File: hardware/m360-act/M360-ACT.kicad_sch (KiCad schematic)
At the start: 26 parts, among them J1 5V do quadro, J2 M360-RF, J3 RJ45 RELES-A, J4 RJ45 RELES-B, J5 RJ45 SENSORES, SW1 Reed, U1 AMS1117-3.3, U2 74HCT244, U3 CD74HC4067, U4 SRV05-4, U5 SRV05-4, U6 SRV05-4, U7 SRV05-4, U8 SRV05-4

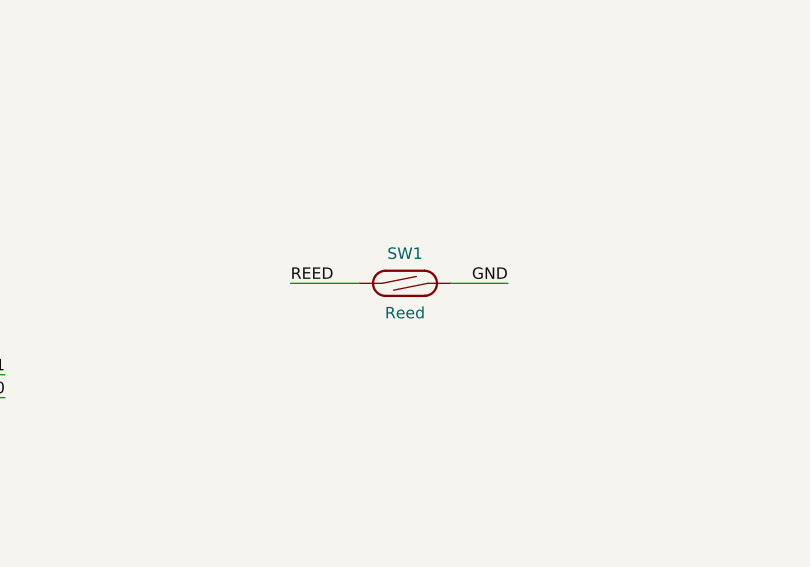
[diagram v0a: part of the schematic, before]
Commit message: feat(hardware): reed vira botão na LP e na ACT — esquemático apenas
⚠️ **ENTREGA PARCIAL: as placas NÃO acompanham.** Os dois `.kicad_pcb` continuam com o reed
`M360:Reed_Littelfuse_59170`. Sincronizar esquemático → placa vai trocar o footprint e
**invalidar o roteamento das duas** (§11.5). Não faça isso sem estar pronto para rerrotear.

O que entra aqui:

- SW1 passa de `Switch:SW_Reed` para `Switch:SW_Push`, footprint
  `Button_Switch_THT:SW_PUSH_6mm`, valor "Repareamento". Os dois símbolos têm pinagem e
  geometria idênticas (pinos 1 e 2 em ±5,08), então a troca não pode alterar a fiação — e o
  `netdiff.py` confirmou: LP 47 redes/182 nós e ACT 63/166, idênticas à base nas duas;
- `place_lp.py`: SW1 de (160, 158) para (160, 153) — o botão ocupa 9,6 × 7,6 mm contra
  11,5 × 2,4 do reed e, em 158, avançaria até y ≈ 164, além da borda em 162;
- `place_act.py`: SW1 sem rotação, e **J1 de rot 90 para rot 0**. O borne abre para −x (as guias
  de fio estão em x ≈ −5,68 no footprint), então em rot 90 a abertura apontava para dentro da
  placa;
- `.kicad_pro` das duas: `track_width` de 0,2 para 0,25 mm, o padrão da família (§11.2). O
  `set_design_rules` do MCP nunca persistiu esse valor — gravava o mínimo.

**Por que parou aqui.** A troca do footprint exige rerroteamento completo, que depende de
`export_dsn`/`import_ses` — e o servidor MCP travou no meio do trabalho: até `get_board_info`
passou a estourar 30 s, dez sondagens seguidas. O `kicad-cli` não exporta nem importa Specctra,
então não há contorno. As placas foram revertidas ao estado commitado e íntegro (LP 552
segmentos/48 vias, ACT 463/23, conferidos contra `bf701dc` e `e94779f`).

Ferramentas novas, todas nascidas deste trabalho:

- `clear_tracks.py` — apaga trilhas e vias para rerrotear do zero;
- `zone_thermals.py` — afina o alívio térmico das zonas;
- `gnd_stitch.py` — via de costura em ilha de plano solta, **com defeito conhecido e
  documentado**: o critério interno de "ilha já ligada" não prova ligação ao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
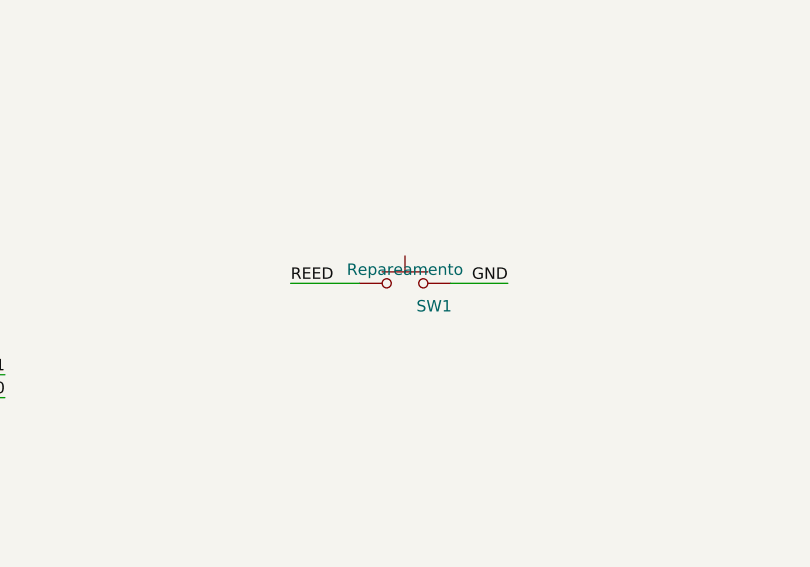
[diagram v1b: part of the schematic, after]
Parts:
- removed SW1: Reed, M360:Reed_Littelfuse_59170, symbol Switch:SW_Reed
- added SW1: Repareamento, Button_Switch_THT:SW_PUSH_6mm, symbol Switch:SW_Push
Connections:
- net GND: now also SW1.2
- net REED: now also SW1.1
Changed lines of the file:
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@@
 	)
 	(symbol
-		(lib_id "Switch:SW_Reed")
-		(at 124.46 209.55 0)
-		(unit 1)
-		(body_style 1)
-		(exclude_from_sim no)
-		(in_bom yes)
-		(on_board yes)
-		(in_pos_files yes)
-		(dnp no)
-		(property "Reference" "SW1"
-			(at 124.46 206.248 0)
-			(show_name no)
-			(do_not_autoplace no)
-			(effects
-				(font
-					(size 1.27 1.27)
-				)
-			)
-		)
-		(property "Value" "Reed"
-			(at 124.46 212.852 0)
-			(show_name no)
-			(do_not_autoplace no)
-			(effects
-				(font
-					(size 1.27 1.27)
-				)
-			)
-		)
-		(property "Footprint" "M360:Reed_Littelfuse_59170"
-			(at 124.46 209.55 0)
-			(hide yes)
-			(show_name no)
-			(do_not_autoplace no)
-			(effects
-				(font
-					(size 1.27 1.27)
-				)
-			)
-		)
-		(property "Datasheet" ""
-			(at 124.46 209.55 0)
-			(hide yes)
-			(show_name no)
-			(do_not_autoplace no)
-			(effects
-				(font
-					(size 1.27 1.27)
-				)
-			)
-		)
-		(property "Description" "reed switch"
-			(at 124.46 209.55 0)
-			(hide yes)
-			(show_name no)
-			(do_not_autoplace no)
-			(effects
-				(font
-					(size 1.27 1.27)
-				)
-			)
-		)
-		(pin "1"
-		)
-		(pin "2"
-		)
-		(instances
-			(project "M360-ACT"
-				(path "/c5ce62f1-25ea-4dcc-94a9-6f847c324d30"
-					(reference "SW1")
-					(unit 1)
-				)
-			)
-		)
-	)
-	(symbol
 		(lib_id "74xx:74HCT244")
 		(at 165.1 124.46 0)
@@
 		)
 	)
+	(symbol
+		(lib_id "Switch:SW_Push")
+		(at 124.46 209.55 0)
+		(unit 1)
+		(body_style 1)
+		(exclude_from_sim no)
+		(in_bom yes)
+		(on_board yes)
+		(in_pos_files yes)
+		(dnp no)
+		(property "Reference" "SW1"
+			(at 125.73 212.09 0)
+			(show_name no)
+			(do_not_autoplace no)
+			(effects
+				(font
+					(size 1.27 1.27)
+				)
+				(justify left)
+			)
+		)
+		(property "Value" "Repareamento"
+			(at 124.46 208.026 0)
+			(show_name no)
+			(do_not_autoplace no)
+			(effects
+				(font
+					(size 1.27 1.27)
+				)
+			)
+		)
+		(property "Footprint" "Button_Switch_THT:SW_PUSH_6mm"
+			(at 124.46 214.63 0)
+			(hide yes)
+			(show_name no)
+			(do_not_autoplace no)
+			(effects
+				(font
+					(size 1.27 1.27)
+				)
+			)
+		)
+		(property "Datasheet" ""
+			(at 124.46 214.63 0)
+			(hide yes)
+			(show_name no)
+			(do_not_autoplace no)
+			(effects
+				(font
+					(size 1.27 1.27)
+				)
+			)
+		)
+		(property "Description" "Push button switch, generic, two pins"
+			(at 124.46 209.55 0)
+			(hide yes)
+			(show_name no)
+			(do_not_autoplace no)
+			(effects
+				(font
+					(size 1.27 1.27)
+				)
+			)
+		)
+		(pin "1"
+		)
+		(pin "2"
+		)
+		(instances
+			(project "M360-ACT"
+				(path "/c5ce62f1-25ea-4dcc-94a9-6f847c324d30"
+					(reference "SW1")
+					(unit 1)
+				)
+			)
+		)
+	)

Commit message: feat(hardware): LP e ACT rerroteadas com o botão; GND volta a ser roteado
Conclui a troca do reed pelo botão iniciada em 0948368, que parou no esquemático.

Placas, para cada uma: del_fp.py SW1 → sincronização com o esquemático → place_*.py →
clear_tracks.py → export_dsn → dsn_sem_plano.py → Freerouting → import_ses →
zone_thermals.py → DRC com refill.

- M360-LP: 572 trilhas, 44 vias. DRC com 0 erros e 0 desconectados; restam os 8
  silk_edge_clearance dos RJ45, que já existiam.
- M360-ACT: 489 trilhas, 24 vias. DRC com 0 erros e 0 desconectados; restam os 13
  silk_edge_clearance, que já existiam. J1 em rot 0, como o place_act.py já pedia.
- Redes de todos os pads conferidas contra o HEAD: só o SW1 mudou. Trilhas todas de 0,25 mm.
- Paridade esquemático × placa com as mesmas contagens da base (237 e 195); some o
  footprint_symbol_mismatch do SW1.

**O GND não era roteado — e era isso que partia o plano.** Com zona de GND na placa, o DSN
declara `plane GND` e o Freerouting não desenha um fio de terra sequer. O primeiro roteamento
(bf701dc, 88 segmentos de GND) foi feito antes de as zonas existirem; todo rerroteamento
posterior perdia esse terra. Rerroteada com o DSN como sai do KiCad, a LP deu 16
unconnected_items, todos "Zona [GND]"; tirando as declarações plane, 0 — 100 segmentos de GND
na LP e 95 na ACT. Explica também os 15 desconectados imóveis da sessão anterior (§11.6).
Novo `tools/dsn_sem_plano.py`, e a §11 corrigida: 11.2, 11.4, 11.5 e 11.6.

Ajustes que o DRC pediu depois do rerroteamento:
- J4 da ACT, pino 8: starved_thermal → ligação sólida (pad_zone_connect.py), como o J3;
- silk_lp.py: referência do SW1 saía sobre "M360-LP"; vai para (172, 155);
- silk_act.py: referência do U1 encostava no J1, agora em rot 0; sobe para y = 143.

Botão: SHOU HAN TS665CJ, C393938, tátil 6 × 6 mm THT, SW1 nas três placas (LP, ACT e GW),
**solda manual e fora do PCBA**. Propriedade LCSC gravada nos três esquemáticos, com netlists
idênticas antes e depois. `add_lcsc.py` g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
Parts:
- SW1: LCSC (none) -> C393938
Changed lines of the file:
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@@
+			)
+		)
+		(property "LCSC" "C393938"
+			(at 124.46 209.55 0)
+			(hide yes)
+			(effects
+				(font
+					(size 1.27 1.27)
+				)
 			)
 		)

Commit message: feat(hardware): peças de solda manual fora do BOM e da posição; C13 da LP corrigido
Novo `tools/solda_manual.py`: marca as duas pontas pela referência — `in_bom no` e
`in_pos_files no` no símbolo, `exclude_from_bom` e `exclude_from_pos_files` no footprint. O BOM
sai do esquemático e a posição sai da placa; marcar um lado só faria a paridade divergir.

Aplicado:
- LP: SW1, J1, J2, A1, J4
- ACT: SW1, J3, J4, J5, A1, J2
- GW: SW1, J1

Conferido exportando BOM e posição antes e depois: saíram exatamente essas peças. Netlists
idênticas nas três; DRC e paridade com as mesmas contagens da base (LP 237, ACT 195, GW 69).
A propriedade LCSC fica nos símbolos, para a compra (§9.1).

**Defeito corrigido:** o C13 da LP (100 nF 0603) carregava o código do reed, C315909, desde
bc651ca — a JLCPCB montaria um reed no lugar do capacitor. Agora C14663, como os demais 100 nF,
pelo `add_lcsc.py --set`.

Também na §9.1: espaçamento de 6,5 × 4,5 mm do TS665CJ confirmado contra o datasheet.

Registrado na §9, sem correção: a ACT e a GW não têm código LCSC em peça nenhuma, e os
PWR_FLAG da GW saem no BOM. Bornes (J1 da ACT, J2 da GW) e JST (J3 da LP e da GW) continuam no
BOM, por não estarem na lista desta decisão.

Co-Authored-By: Claude Opus 5 (1M context) <noreply@anthropic.com>
Claude-Session: https://claude.ai/code/session_012t7RkcrXvvpDVjKVimNu18
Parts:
- A1, J2, J3, J4, J5, SW1: now left out of the parts list
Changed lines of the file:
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@@
 		(body_style 1)
 		(exclude_from_sim no)
-		(in_bom yes)
+		(in_bom no)
 		(on_board yes)
-		(in_pos_files yes)
+		(in_pos_files no)
 		(dnp no)
 		(property "Reference" "A1"
@@
 		(body_style 1)
 		(exclude_from_sim no)
-		(in_bom yes)
+		(in_bom no)
 		(on_board yes)
-		(in_pos_files yes)
+		(in_pos_files no)
 		(dnp no)
 		(property "Reference" "J2"
@@
 		(body_style 1)
 		(exclude_from_sim no)
-		(in_bom yes)
+		(in_bom no)
 		(on_board yes)
-		(in_pos_files yes)
+		(in_pos_files no)
 		(dnp no)
 		(property "Reference" "J3"
@@
 		(body_style 1)
 		(exclude_from_sim no)
-		(in_bom yes)
+		(in_bom no)
 		(on_board yes)
-		(in_pos_files yes)
+		(in_pos_files no)
 		(dnp no)
 		(property "Reference" "J4"
@@
 		(body_style 1)
 		(exclude_from_sim no)
-		(in_bom yes)
+		(in_bom no)
 		(on_board yes)
-		(in_pos_files yes)
+		(in_pos_files no)
 		(dnp no)
 		(property "Reference" "J5"
@@
 		(body_style 1)
 		(exclude_from_sim no)
-		(in_bom yes)
+		(in_bom no)
 		(on_board yes)
-		(in_pos_files yes)
+		(in_pos_files no)
 		(dnp no)
 		(property "Reference" "SW1"

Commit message: feat(hardware): códigos LCSC na M360-ACT e na M360-GW
Até aqui só a LP tinha código: o `add_lcsc.py` conhece apenas o mapa dela. Gravados com
`add_lcsc.py --set`, cada código conferido no catálogo local (estoque, encapsulamento, tipo).
Netlists idênticas antes e depois nas duas placas.

ACT — todas as peças, menos o Pro Mini (como na LP):
- C1, C3 10 µF 0805 C15850 · C2, C4–C6 100 nF C14663 · C7 1 nF C1588 — basic
- R1–R3 10 kΩ C25804 · R4 20 kΩ C4184 — basic
- U1 AMS1117-3.3 C6186 (basic) · U2 74HCT244 C5978 · U3 CD74HC4067 C496123 · U4–U8 SRV05-4 C558418
- J1 borne C8465 · J2 soquete C492399 · J3–J5 RJ45 C385834

GW — toda THT, sem nenhuma basic:
- C1 10 µF eletrolítico D5 P2 C106654 · C2–C4 100 nF C84772
- R1–R3 1 kΩ C57435 · R4 10 kΩ C57436 (UNI-ROYAL, axial 1/4 W 1 %)
- J1 soquete C492399 · J2 borne C8465 · J3 JST B6B-XH-A C144397
- U1 D1 mini sem código: não existe no catálogo.

O 100 nF da GW é MLCC X7R com terminais, não disco: os discos em estoque são Y5V, que perdem
boa parte da capacitância com tensão e temperatura.

Atenção: o C25804 (10 kΩ) não está no catálogo de peças em estoque, e não há outro 10 kΩ 0603
basic — a alternativa é extended (C2906982). Afeta 11 posições da LP e 3 da ACT; registrado na
§9 para confirmar no site antes do pedido. §9.1 ganha as peças novas.

Co-Authored-By: Claude Opus 5 (1M context) <noreply@anthropic.com>
Claude-Session: https://claude.ai/code/session_012t7RkcrXvvpDVjKVimNu18
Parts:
- C1, C3: LCSC (none) -> C15850
- C2, C4, C5, C6: LCSC (none) -> C14663
- C7: LCSC (none) -> C1588
- J1: LCSC (none) -> C8465
- J2: LCSC (none) -> C492399
- J3, J4, J5: LCSC (none) -> C385834
- R1, R2, R3: LCSC (none) -> C25804
- R4: LCSC (none) -> C4184
- U1: LCSC (none) -> C6186
- U2: LCSC (none) -> C5978
- U3: LCSC (none) -> C496123
- U4, U5, U6, U7, U8: LCSC (none) -> C558418
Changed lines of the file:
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@@
+			)
+		)
+		(property "LCSC" "C8465"
+			(at 30.48 44.45 0)
+			(hide yes)
+			(effects
+				(font
+					(size 1.27 1.27)
+				)
 			)
 		)
@@
 			)
 		)
+		(property "LCSC" "C15850"
+			(at 48.26 58.42 0)
+			(hide yes)
+			(effects
+				(font
+					(size 1.27 1.27)
+				)
+			)
+		)
 		(property "Datasheet" ""
 			(at 48.26 58.42 0)
@@
 			)
 		)
+		(property "LCSC" "C14663"
+			(at 58.42 58.42 0)
+			(hide yes)
+			(effects
+				(font
+					(size 1.27 1.27)
+				)
+			)
+		)
 		(property "Datasheet" ""
 			(at 58.42 58.42 0)
@@
 			)
 		)
+		(property "LCSC" "C6186"
+			(at 74.93 44.45 0)
+			(hide yes)
+			(effects
+				(font
+					(size 1.27 1.27)
+				)
+			)
+		)
 		(property "Datasheet" "http://www.advanced-monolithic.com/pdf/ds1117.pdf"
 			(at 77.47 38.1 0)
@@
 			)
 		)
+		(property "LCSC" "C15850"
+			(at 95.25 58.42 0)
+			(hide yes)
+			(effects
+				(font
+					(size 1.27 1.27)
+				)
+			)
+		)
 		(property "Datasheet" ""
 			(at 95.25 58.42 0)
@@
 			)
 		)
+		(property "LCSC" "C14663"
+			(at 105.41 58.42 0)
+			(hide yes)
+			(effects
+				(font
+					(size 1.27 1.27)
+				)
+			)
+		)
 		(property "Datasheet" ""
 			(at 105.41 58.42 0)
@@
 			)
 		)
+		(property "LCSC" "C25804"
+			(at 101.6 119.38 0)
+			(hide yes)
+			(effects
+				(font
+					(size 1.27 1.27)
+				)
+			)
+		)
 		(property "Datasheet" ""
 			(at 101.6 119.38 0)
@@
 			)
 		)
+		(property "LCSC" "C492399"
+			(at 64.77 224.79 0)
+			(hide yes)
+			(effects
+				(font
+					(size 1.27 1.27)
+				)
+			)
+		)
 		(property "Datasheet" ""
 			(at 64.77 224.79 0)
@@
 			)
 		)
+		(property "LCSC" "C5978"
+			(at 165.1 124.46 0)
+			(hide yes)
+			(effects
+				(font
+					(size 1.27 1.27)
+				)
+			)
+		)
 		(property "Datasheet" "https://assets.nexperia.com/documents/data-sheet/74HC_HCT244.pdf"
 			(at 165.1 124.46 0)
@@
 			)
 		)
+		(property "LCSC" "C25804"
+			(at 134.62 87.63 0)
+			(hide yes)
+			(effects
+				(font
+					(size 1.27 1.27)
+				)
+			)
+		)
 		(property "Datasheet" ""
 			(at 134.62 87.63 0)
@@
 			)
 		)
+		(property "LCSC" "C14663"
+			(at 185.42 91.44 0)
+			(hide yes)
+			(effects
+				(font
+					(size 1.27 1.27)
+				)
+			)
+		)
 		(property "Datasheet" ""
 			(at 185.42 91.44 0)
@@
 			)
 		)
+		(property "LCSC" "C496123"
+			(at 247.65 139.7 0)
+			(hide yes)
+			(effects
+				(font
+					(size 1.27 1.27)
+				)
+			)
+		)
 		(property "Datasheet" "http://www.ti.com/lit/ds/symlink/cd74hc4067.pdf"
 			(at 238.76 161.29 0)
@@
 			)
 		)
+		(property "LCSC" "C14663"
+			(at 267.97 100.33 0)
+			(hide yes)
+			(effects
+				(font
+					(size 1.27 1.27)
+				)
+			)
+		)
 		(property "Datasheet" ""
 			(at 267.97 100.33 0)
@@
 			)
 		)
+		(property "LCSC" "C25804"
+			(at 284.48 237.49 0)
+			(hide yes)
+			(effects
+				(font
+					(size 1.27 1.27)
+				)
+			)
+		)
 		(property "Datasheet" ""
 			(at 284.48 237.49 0)
@@
 			)
 		)
+		(property "LCSC" "C4184"
+			(at 284.48 252.73 0)
+			(hide yes)
+			(effects
+				(font
+					(size 1.27 1.27)
+				)
+			)
+		)
 		(property "Datasheet" ""
 			(at 284.48 252.73 0)
@@
 			)
 		)
+		(property "LCSC" "C1588"
+			(at 298.45 247.65 0)
+			(hide yes)
+			(effects
+				(font
+					(size 1.27 1.27)
+				)
+			)
+		)
 		(property "Datasheet" ""
 			(at 298.45 247.65 0)
@@
 			)
 		)
+		(property "LCSC" "C558418"
+			(at 314.96 49.53 0)
+			(hide yes)
+			(effects
+				(font
+					(size 1.27 1.27)
+				)
+			)
+		)
 		(property "Datasheet" "http://www.onsemi.com/pub/Collateral/SRV05-4-D.PDF"
 			(at 314.96 49.53 0)
@@
 			)
 		)
+		(property "LCSC" "C558418"
+			(at 314.96 90.17 0)
+			(hide yes)
+			(effects
+				(font
+					(size 1.27 1.27)
+				)
+			)
+		)
 		(property "Datasheet" "http://www.onsemi.com/pub/Collateral/SRV05-4-D.PDF"
 			(at 314.96 90.17 0)
@@
 			)
 		)
+		(property "LCSC" "C558418"
+			(at 314.96 139.7 0)
+			(hide yes)
+			(effects
+				(font
+					(size 1.27 1.27)
+				)
+			)
+		)
 		(property "Datasheet" "http://www.onsemi.com/pub/Collateral/SRV05-4-D.PDF"
 			(at 314.96 139.7 0)
@@
 			)
 		)
+		(property "LCSC" "C558418"
+			(at 314.96 180.34 0)
+			(hide yes)
+			(effects
+				(font
+					(size 1.27 1.27)
+				)
+			)
+		)
 		(property "Datasheet" "http://www.onsemi.com/pub/Collateral/SRV05-4-D.PDF"
 			(at 314.96 180.34 0)
@@
 			)
 		)
+		(property "LCSC" "C558418"
+			(at 314.96 234.95 0)
+			(hide yes)
+			(effects
+				(font
+					(size 1.27 1.27)
+				)
+			)
+		)
 		(property "Datasheet" "http://www.onsemi.com/pub/Collateral/SRV05-4-D.PDF"
 			(at 314.96 234.95 0)
@@
 			)
 		)
+		(property "LCSC" "C385834"
+			(at 364.49 62.23 0)
+			(hide yes)
+			(effects
+				(font
+					(size 1.27 1.27)
+				)
+			)
+		)
 		(property "Datasheet" ""
 			(at 364.49 62.865 90)
@@
 			)
 		)
+		(property "LCSC" "C385834"
+			(at 364.49 137.16 0)
+			(hide yes)
+			(effects
+				(font
+					(size 1.27 1.27)
+				)
+			)
+		)
 		(property "Datasheet" ""
 			(at 364.49 137.795 90)
@@
 			(effects
 				(font
+					(size 1.27 1.27)
+				)
+			)
+		)
+		(property "LCSC" "C385834"
+			(at 364.49 214.63 0)
+			(hide yes)
+			(effects
+				(font
